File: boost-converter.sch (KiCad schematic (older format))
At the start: 32 parts, among them Q1 STP33N65M2, U2 MAX1771, U3 CAT5171, U4 HV7802

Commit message: Fix broken symbols and DRC tests
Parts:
- Q1: symbol IRF644PBF -> sci-bots:IRF644PBF
- U2: symbol MAX1771 -> sci-bots:MAX1771
- U3: symbol CAT5171 -> sci-bots:CAT5171
- U4: symbol HV7802 -> sci-bots:HV7802
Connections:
- wire segments 55 -> 83
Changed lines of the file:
@@
 $EndComp
 $Comp
-L MAX1771 U2
+L sci-bots:MAX1771 U2
 U 1 1 56BE960B
 P 3600 4350
@@
 $EndComp
 $Comp
-L IRF644PBF Q1
+L sci-bots:IRF644PBF Q1
 U 1 1 56BE960C
 P 4600 4150
@@
 A1/HV_FB
 $Comp
-L HV7802 U4
+L sci-bots:HV7802 U4
 U 1 1 56BEB19A
 P 8400 4450
@@
 A3/MAX1771_CS
 $Comp
-L CAT5171 U3
+L sci-bots:CAT5171 U3
 U 1 1 58493EBB
 P 6400 4600
@@
 Connection ~ 3600 5150
 Wire Wire Line
-	4700 3400 4700 3950
+	4700 3400 4700 3700
 Connection ~ 4700 5150
 Wire Wire Line
@@
 Wire Wire Line
 	4350 4350 4700 4350
-Connection ~ 4700 4350
 Wire Wire Line
 	2900 5150 2900 4900
@@
 Connection ~ 5350 5150
 Wire Wire Line
-	4100 4500 6000 4500
+	4100 4500 5650 4500
 Connection ~ 5950 3700
 Wire Wire Line
@@
 	6400 4200 6400 4100
 Wire Wire Line
-	6700 4100 6900 4100
-Wire Wire Line
-	2200 5150 8550 5150
-Wire Wire Line
-	5200 3700 8400 3700
+	6700 4100 6750 4100
+Wire Wire Line
+	2200 5150 2500 5150
+Wire Wire Line
+	5200 3700 5350 3700
 Wire Wire Line
 	7650 4850 7650 4150
@@
 	2500 3700 2500 3400
 Wire Wire Line
-	2200 3400 4100 3400
+	2200 3400 2500 3400
 Wire Wire Line
 	2750 3700 2750 3400
@@
 Wire Wire Line
 	2900 4300 3100 4300
-Wire Wire Line
-	2750 4000 2750 4000
 Wire Wire Line
 	2750 4000 2750 5150
@@
 	5350 3400 5300 3400
 Wire Wire Line
-	5350 3400 5350 4150
+	5350 3400 5350 3700
 Wire Wire Line
 	6800 4500 6950 4500
@@
 	5950 4700 6000 4700
 Wire Wire Line
-	5950 4250 5950 4600
+	5950 4250 5950 4500
 Connection ~ 5950 4500
 Wire Wire Line
@@
 	5650 3700 5650 3950
 Wire Wire Line
-	5650 4250 5650 4700
+	5650 4250 5650 4500
 $Comp
 L Device:C C21
@@
 	1    0    0    -1
 $EndComp
+Wire Wire Line
+	3600 5150 4700 5150
+Wire Wire Line
+	4700 5150 5350 5150
+Wire Wire Line
+	4700 3700 4700 3950
+Wire Wire Line
+	5950 5150 6400 5150
+Wire Wire Line
+	6400 5150 6800 5150
+Wire Wire Line
+	5350 3700 5650 3700
+Wire Wire Line
+	5350 3700 5350 4150
+Wire Wire Line
+	5350 5150 5650 5150
+Wire Wire Line
+	5950 3700 7650 3700
+Wire Wire Line
+	7650 5150 8250 5150
+Wire Wire Line
+	7650 3700 8150 3700
+Wire Wire Line
+	8250 5150 8550 5150
+Wire Wire Line
+	8150 3700 8400 3700
+Wire Wire Line
+	2900 5150 3100 5150
+Wire Wire Line
+	2750 3400 3600 3400
+Wire Wire Line
+	2750 5150 2900 5150
+Wire Wire Line
+	3100 5150 3600 5150
+Wire Wire Line
+	6750 4100 6900 4100
+Wire Wire Line
+	7250 5150 7650 5150
+Wire Wire Line
+	6800 5150 7250 5150
+Wire Wire Line
+	5950 4500 6000 4500
+Wire Wire Line
+	5950 4500 5950 4600
+Wire Wire Line
+	5650 4500 5950 4500
+Wire Wire Line
+	5650 4500 5650 4700
+Wire Wire Line
+	5650 5150 5950 5150
+Wire Wire Line
+	5650 3700 5950 3700
+Wire Wire Line
+	2500 3400 2750 3400
+Wire Wire Line
+	2500 5150 2750 5150
+Wire Wire Line
+	3600 3400 4100 3400
 $EndSCHEMATC

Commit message: Update BOM
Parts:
- C1: MPN (none) -> T494D106M025AT; Manufacturer (none) -> KEMET
- C19, C21: MPN (none) -> CL21C101JECNNWC; Manufacturer (none) -> Samsung
- C2, C5, C8: MPN (none) -> CL21B104KBCNNNC; Manufacturer (none) -> Samsung
- C24: MPN (none) -> 501R15W102KV4E; Manufacturer (none) -> Johanson
- C30, C31: MPN (none) -> CL21C151JBANNNC; Manufacturer (none) -> Samsung
- C6: MPN (none) -> T491X107K025AT; Manufacturer (none) -> KEMET
- C7: MPN (none) -> EEV-EB2G3R3Q; Manufacturer (none) -> Panasonic
- D1: MPN (none) -> VS-4EGU06-M3/5BT; Manufacturer (none) -> Vishay
- L1: MPN (none) -> SRR1210-470M; Manufacturer (none) -> Bourns
- Q1: MPN (none) -> STP33N65M2; Manufacturer (none) -> STMicroelectronics
- R13: MPN (none) -> RC0805FR-075K1L; Manufacturer (none) -> Yageo
- R14: MPN (none) -> ERJ-6DQJ1R0V; Manufacturer (none) -> Panasonic
- R15: MPN (none) -> RC0805FR-0751KL; Manufacturer (none) -> Yageo
- R16: MPN (none) -> RC0805FR-07100KL; Manufacturer (none) -> Yageo
- R38, R39: MPN (none) -> RC0805FR-0710RL; Manufacturer (none) -> Yageo
- R46, R47: MPN (none) -> RC0805FR-0751RL; Manufacturer (none) -> Yageo
- R48, R49: MPN (none) -> RC0805FR-07150RL; Manufacturer (none) -> Yageo
- R5: MPN (none) -> CSR2512C0R03F; Manufacturer (none) -> Riedon
- R6, R8: MPN (none) -> HVCB1206KDL2M00; Manufacturer (none) -> Stackpole Electronics
- R7: MPN (none) -> RC0805FR-0710KL; Manufacturer (none) -> Yageo
- R9: MPN (none) -> RC0805FR-0720KL; Manufacturer (none) -> Yageo
- U2: MPN (none) -> MAX1771ESA+; Manufacturer (none) -> Maxim Integrated
- U3: MPN (none) -> CAT5171TBI-50GT3; Manufacturer (none) -> onsemi
- U4: MPN (none) -> HV7802MG-G; Manufacturer (none) -> Microchip

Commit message: Remove "Mfg_Part_No" field (replaced by  "MPN")
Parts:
- C1: Mfg_Part_No T494D106M025AT -> (none)
- C2, C5, C8: Mfg_Part_No CL21B104KBCNNNC -> (none)
- C24: Mfg_Part_No 501R15W102KV4E -> (none)
- C30, C31: Mfg_Part_No CL21C151JBANNNC -> (none)
- C6: Mfg_Part_No T491X107K025AT -> (none)
- C7: Mfg_Part_No EEV-EB2G3R3Q -> (none)
- D1: Mfg_Part_No VS-4EGU06-M3/5BT -> (none)
- L1: Mfg_Part_No SRR1210-470M -> (none)
- Q1: Mfg_Part_No STP33N65M2 -> (none)
- R13: Mfg_Part_No RC0805FR-075K1L -> (none)
- R14: Mfg_Part_No ERJ-6DQJ1R0V -> (none)
- R15: Mfg_Part_No RC0805FR-0751KL -> (none)
- R16: Mfg_Part_No RC0805FR-07100KL -> (none)
- R38, R39: Mfg_Part_No RC0805FR-0710RL -> (none)
- R46, R47: Mfg_Part_No RC0805FR-0751RL -> (none)
- R48, R49: Mfg_Part_No RC0805FR-07150RL -> (none)
- R5: Mfg_Part_No CSR2512C0R03F -> (none)
- R6, R8: Mfg_Part_No HVCB1206KDL2M00 -> (none)
- R7: Mfg_Part_No RC0805FR-0710KL -> (none)
- R9: Mfg_Part_No RC0805FR-0720KL -> (none)
- U2: Mfg_Part_No MAX1771ESA+ -> (none)
- U3: Mfg_Part_No CAT5171TBI-50GT3 -> (none)
- U4: Mfg_Part_No HV7802MG-G -> (none)
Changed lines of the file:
@@
 F 4 "CL21B104KBCNNNC" H 2925 4950 50 0001 C CNN "MPN"
 F 5 "Samsung" H 2925 4950 50 0001 C CNN "Manufacturer"
-F 6 "CL21B104KBCNNNC" H 2900 4750 60 0001 C CNN "Mfg_Part_No"
 	1    2900 4750
 	1    0    0    -1
@@
 F 4 "T491X107K025AT" H 2225 4050 50 0001 C CNN "MPN"
 F 5 "KEMET" H 2225 4050 50 0001 C CNN "Manufacturer"
-F 6 "T491X107K025AT" H 2200 3850 60 0001 C CNN "Mfg_Part_No"
 	1    2200 3850
 	1    0    0    -1
@@
 F 4 "SRR1210-470M" H 4200 3500 50 0001 C CNN "MPN"
 F 5 "Bourns" H 4200 3500 50 0001 C CNN "Manufacturer"
-F 6 "SRR1210-470M" H 4250 3400 60 0001 C CNN "Mfg_Part_No"
 	1    4250 3400
 	0    1    1    0
@@
 F 4 "VS-4EGU06-M3/5BT" H 5050 3900 50 0001 C CNN "MPN"
 F 5 "Vishay" H 5050 3900 50 0001 C CNN "Manufacturer"
-F 6 "VS-4EGU06-M3/5BT" H 5050 3700 60 0001 C CNN "Mfg_Part_No"
 	1    5050 3700
 	-1   0    0    1
@@
 F 4 "EEV-EB2G3R3Q" H 5375 4500 50 0001 C CNN "MPN"
 F 5 "Panasonic" H 5375 4500 50 0001 C CNN "Manufacturer"
-F 6 "EEV-EB2G3R3Q" H 5350 4300 60 0001 C CNN "Mfg_Part_No"
 	1    5350 4300
 	1    0    0    -1
@@
 F 4 "RC0805FR-0710KL" H 6030 5050 50 0001 C CNN "MPN"
 F 5 "Yageo" H 6030 5050 50 0001 C CNN "Manufacturer"
-F 6 "RC0805FR-0710KL" H 5950 4950 60 0001 C CNN "Mfg_Part_No"
 	1    5950 4950
 	1    0    0    -1
@@
 F 4 "HVCB1206KDL2M00" H 5850 4200 50 0001 C CNN "MPN"
 F 5 "Stackpole Electronics" H 5850 4200 50 0001 C CNN "Manufacturer"
-F 6 "HVCB1206KDL2M00" H 5950 4100 60 0001 C CNN "Mfg_Part_No"
 	1    5950 4100
 	1    0    0    -1
@@
 F 4 "MAX1771ESA+ " H 3400 4200 50 0001 C CNN "MPN"
 F 5 "Maxim Integrated" H 3400 4200 50 0001 C CNN "Manufacturer"
-F 6 "MAX1771ESA+ " H 3600 4350 60 0001 C CNN "Mfg_Part_No"
 	1    3600 4350
 	1    0    0    -1
@@
 F 4 "STP33N65M2" H 4750 4250 50 0001 C CNN "MPN"
 F 5 "STMicroelectronics" H 4750 4250 50 0001 C CNN "Manufacturer"
-F 6 "STP33N65M2" H 4600 4150 60 0001 C CNN "Mfg_Part_No"
 	1    4600 4150
 	1    0    0    -1
@@
 F 4 "CSR2512C0R03F" H 4780 5100 50 0001 C CNN "MPN"
 F 5 "Riedon" H 4780 5100 50 0001 C CNN "Manufacturer"
-F 6 "CSR2512C0R03F" H 4700 5000 60 0001 C CNN "Mfg_Part_No"
 	1    4700 5000
 	1    0    0    -1
@@
 F 4 "HVCB1206KDL2M00" H 7730 4100 50 0001 C CNN "MPN"
 F 5 "Stackpole Electronics" H 7730 4100 50 0001 C CNN "Manufacturer"
-F 6 "HVCB1206KDL2M00" H 7650 4000 60 0001 C CNN "Mfg_Part_No"
 	1    7650 4000
 	-1   0    0    1
@@
 F 4 "RC0805FR-0720KL" H 7730 5100 50 0001 C CNN "MPN"
 F 5 "Yageo" H 7730 5100 50 0001 C CNN "Manufacturer"
-F 6 "RC0805FR-0720KL" H 7650 5000 60 0001 C CNN "Mfg_Part_No"
 	1    7650 5000
 	-1   0    0    1
@@
 F 4 "HV7802MG-G" H 8400 4200 50 0001 C CNN "MPN"
 F 5 "Microchip" H 8400 4200 50 0001 C CNN "Manufacturer"
-F 6 "HV7802MG-G" H 8400 4450 60 0001 C CNN "Mfg_Part_No"
 	1    8400 4450
 	1    0    0    -1
@@
 F 4 "RC0805FR-075K1L" H 8300 4000 50 0001 C CNN "MPN"
 F 5 "Yageo" H 8300 4000 50 0001 C CNN "Manufacturer"
-F 6 "RC0805FR-075K1L" H 8400 3900 60 0001 C CNN "Mfg_Part_No"
 	1    8400 3900
 	1    0    0    -1
@@
 F 4 "ERJ-6DQJ1R0V" H 8450 3800 50 0001 C CNN "MPN"
 F 5 "Panasonic" H 8450 3800 50 0001 C CNN "Manufacturer"
-F 6 "ERJ-6DQJ1R0V" H 8550 3700 60 0001 C CNN "Mfg_Part_No"
 	1    8550 3700
 	0    1    1    0
@@
 F 4 "RC0805FR-07100KL" H 8600 4000 50 0001 C CNN "MPN"
 F 5 "Yageo" H 8600 4000 50 0001 C CNN "Manufacturer"
-F 6 "RC0805FR-07100KL" H 8700 3900 60 0001 C CNN "Mfg_Part_No"
 	1    8700 3900
 	-1   0    0    1
@@
 F 4 "RC0805FR-0751KL" H 8630 5100 50 0001 C CNN "MPN"
 F 5 "Yageo" H 8630 5100 50 0001 C CNN "Manufacturer"
-F 6 "RC0805FR-0751KL" H 8550 5000 60 0001 C CNN "Mfg_Part_No"
 	1    8550 5000
 	-1   0    0    1
@@
 F 4 "CL21B104KBCNNNC" H 6500 4250 50 0001 C CNN "MPN"
 F 5 "Samsung" H 6500 4250 50 0001 C CNN "Manufacturer"
-F 6 "CL21B104KBCNNNC" H 6550 4100 60 0001 C CNN "Mfg_Part_No"
 	1    6550 4100
 	0    1    1    0
@@
 F 4 "T494D106M025AT" H 2525 4050 50 0001 C CNN "MPN"
 F 5 "KEMET" H 2525 4050 50 0001 C CNN "Manufacturer"
-F 6 "T494D106M025AT" H 2500 3850 60 0001 C CNN "Mfg_Part_No"
 	1    2500 3850
 	1    0    0    -1
@@
 F 4 "CAT5171TBI-50GT3" H 6150 5050 50 0001 C CNN "MPN"
 F 5 "onsemi" H 6150 5050 50 0001 C CNN "Manufacturer"
-F 6 "CAT5171TBI-50GT3" H 6400 4600 60 0001 C CNN "Mfg_Part_No"
 	1    6400 4600
 	-1   0    0    -1
@@
 F 4 "RC0805FR-0710RL" H 4150 4300 50 0001 C CNN "MPN"
 F 5 "Yageo" H 4150 4300 50 0001 C CNN "Manufacturer"
-F 6 "RC0805FR-0710RL" H 4250 4200 60 0001 C CNN "Mfg_Part_No"
 	1    4250 4200
 	0    1    1    0
@@
 F 4 "RC0805FR-0710RL" H 4950 3500 50 0001 C CNN "MPN"
 F 5 "Yageo" H 4950 3500 50 0001 C CNN "Manufacturer"
-F 6 "RC0805FR-0710RL" H 4850 3400 60 0001 C CNN "Mfg_Part_No"
 	1    4850 3400
 	0    1    1    0
@@
 F 4 "501R15W102KV4E" H 5100 3550 50 0001 C CNN "MPN"
 F 5 "Johanson" H 5100 3550 50 0001 C CNN "Manufacturer"
-F 6 "501R15W102KV4E" H 5150 3400 60 0001 C CNN "Mfg_Part_No"
 	1    5150 3400
 	0    1    1    0
@@
 F 4 "CL21C151JBANNNC" H 7050 4500 50 0001 C CNN "MPN"
 F 5 "Samsung" H 7050 4500 50 0001 C CNN "Manufacturer"
-F 6 "CL21C151JBANNNC" H 7250 4400 60 0001 C CNN "Mfg_Part_No"
 	1    7250 4400
 	-1   0    0    1
@@
 F 4 "RC0805FR-0751RL" H 7050 4400 50 0001 C CNN "MPN"
 F 5 "Yageo" H 7050 4400 50 0001 C CNN "Manufacturer"
-F 6 "RC0805FR-0751RL" H 7100 4500 60 0001 C CNN "Mfg_Part_No"
 	1    7100 4500
 	0    1    1    0
@@
 F 4 "RC0805FR-0751RL" H 7050 4500 50 0001 C CNN "MPN"
 F 5 "Yageo" H 7050 4500 50 0001 C CNN "Manufacturer"
-F 6 "RC0805FR-0751RL" H 7100 4600 60 0001 C CNN "Mfg_Part_No"
 	1    7100 4600
 	0    1    1    0
@@
 F 4 "CL21C151JBANNNC" H 7050 4800 50 0001 C CNN "MPN"
 F 5 "Samsung" H 7050 4800 50 0001 C CNN "Manufacturer"
-F 6 "CL21C151JBANNNC" H 7250 4700 60 0001 C CNN "Mfg_Part_No"
 	1    7250 4700
 	-1   0    0    1
@@
 F 4 "RC0805FR-07150RL" H 7300 4750 50 0001 C CNN "MPN"
 F 5 "Yageo" H 7300 4750 50 0001 C CNN "Manufacturer"
-F 6 "RC0805FR-07150RL" H 7400 4500 60 0001 C CNN "Mfg_Part_No"
 	1    7400 4500
 	0    1    1    0
@@
 F 4 "RC0805FR-07150RL" H 7500 4850 50 0001 C CNN "MPN"
 F 5 "Yageo" H 7500 4850 50 0001 C CNN "Manufacturer"
-F 6 "RC0805FR-07150RL" H 7400 4600 60 0001 C CNN "Mfg_Part_No"
 	1    7400 4600
 	0    1    1    0
@@
 F 4 "CL21B104KBCNNNC" H 2600 3850 50 0001 C CNN "MPN"
 F 5 "Samsung" H 2600 3850 50 0001 C CNN "Manufacturer"
-F 6 "CL21B104KBCNNNC" H 2750 3850 60 0001 C CNN "Mfg_Part_No"
 	1    2750 3850
 	-1   0    0    1

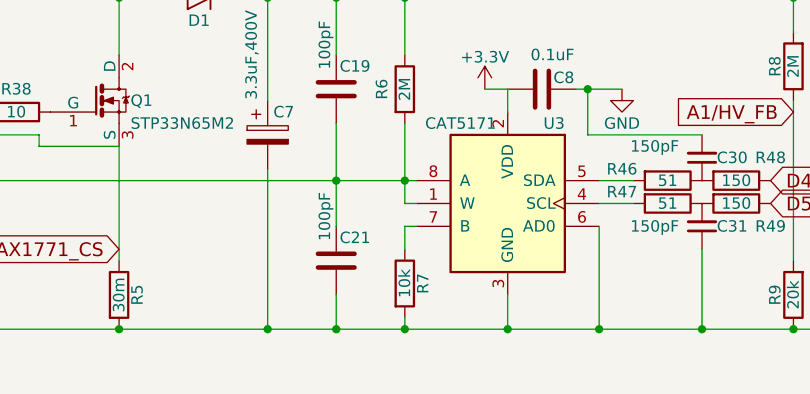
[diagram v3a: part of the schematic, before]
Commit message: Fix #2: Replace R7 with 9.1k resistor
This should ensure that the max voltage is >140V.
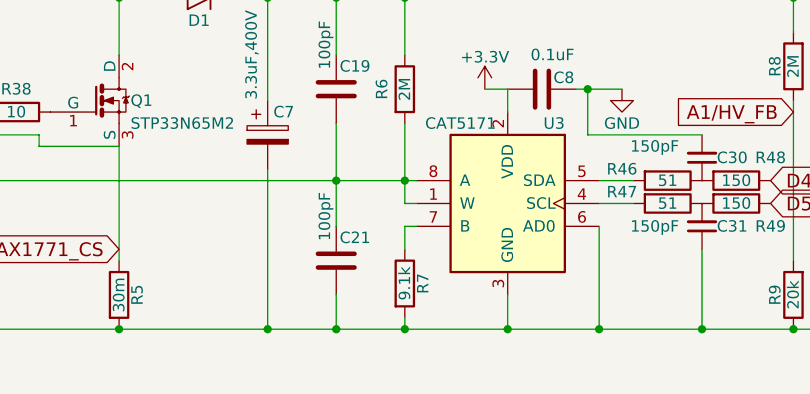
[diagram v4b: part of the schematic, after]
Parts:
- R7: value 10k -> 9.1k; MPN RC0805FR-0710KL -> RC0805FR-079K1L
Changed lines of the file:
@@
 P 5950 4950
 F 0 "R7" V 6030 4950 50 0000 C CNN
-F 1 "10k" V 5950 4950 50 0000 C CNN
+F 1 "9.1k" V 5950 4950 50 0000 C CNN
 F 2 "Resistors_SMD:R_0805" V 5880 4950 30 0001 C CNN
 F 3 "" H 5950 4950 30 0000 C CNN
-F 4 "RC0805FR-0710KL" H 6030 5050 50 0001 C CNN "MPN"
+F 4 "RC0805FR-079K1L" H 6030 5050 50 0001 C CNN "MPN"
 F 5 "Yageo" H 6030 5050 50 0001 C CNN "Manufacturer"
 	1    5950 4950
